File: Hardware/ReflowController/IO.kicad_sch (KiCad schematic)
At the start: 18 parts, among them U5 SZNUD3124DMT1G, U6 VNQ5160K-E

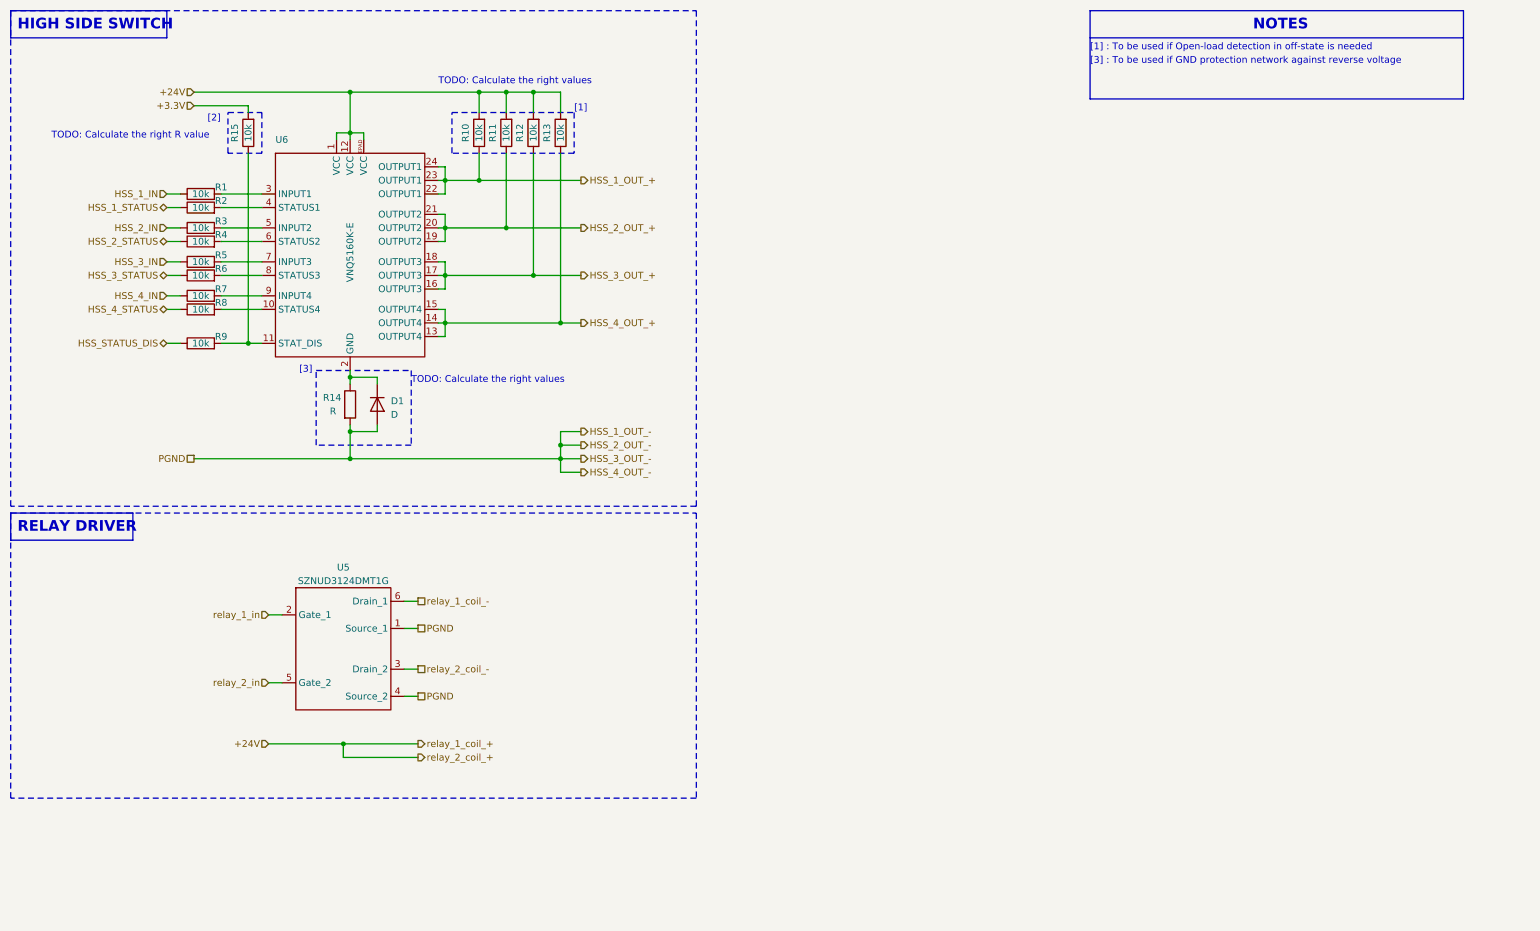
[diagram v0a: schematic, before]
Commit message: added the schematic of the updated pwerAndUi branch(with uC schematic update
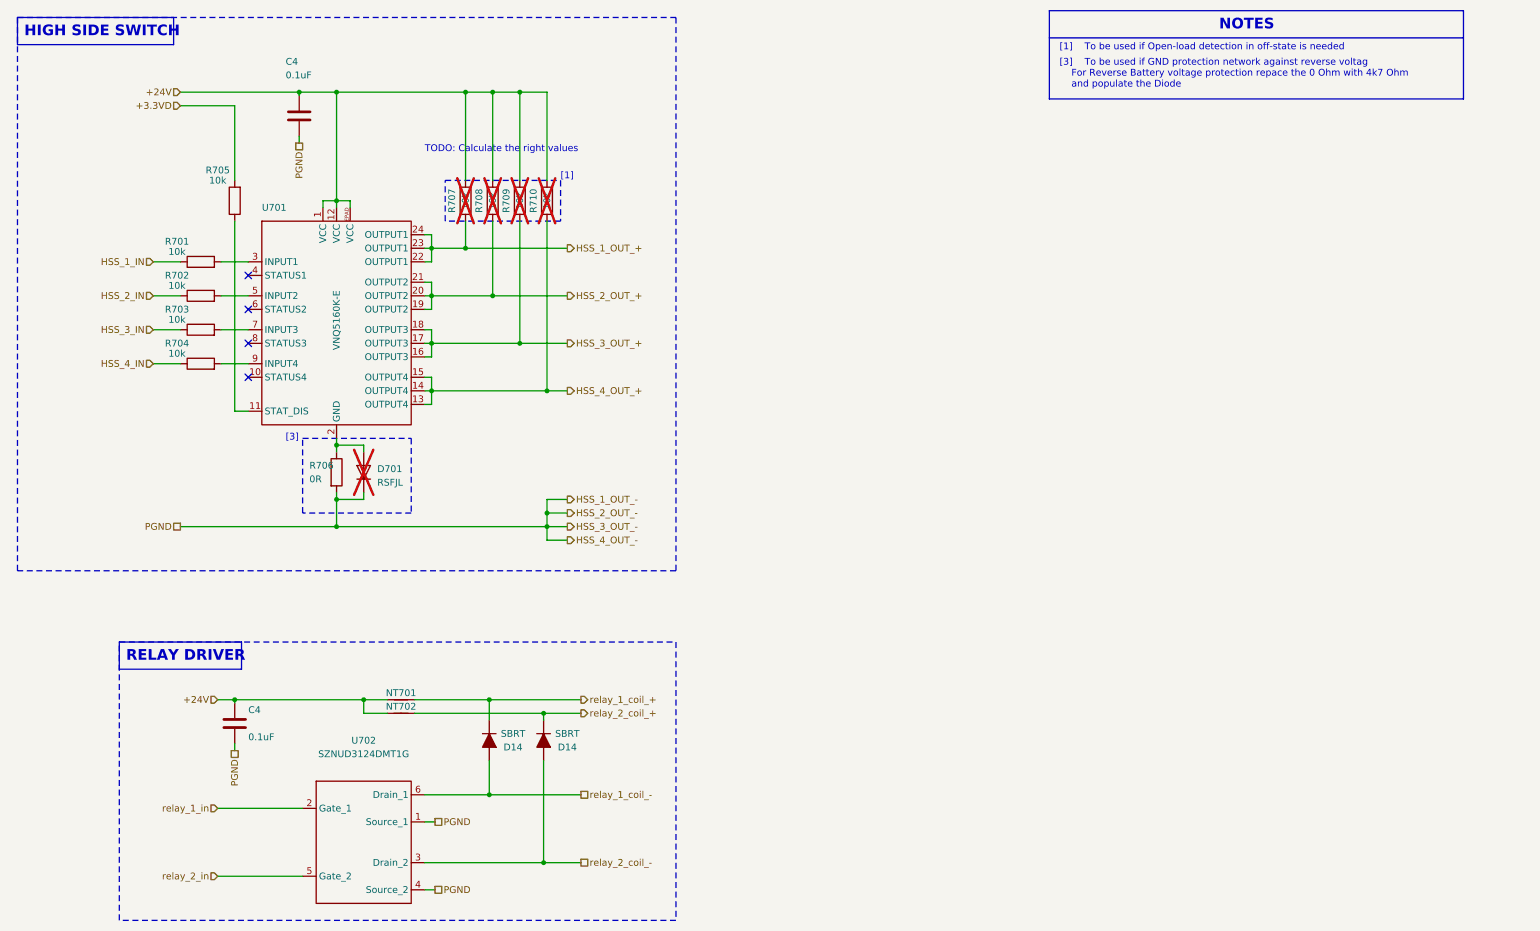
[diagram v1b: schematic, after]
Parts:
- removed R11, R12, R13, R15, R2, R4, R6, R8, R9: 10k, Resistor_SMD:R_0603_1608Metric_Pad0.98x0.95mm_HandSolder, symbol Device:R
- added C4 (x2): 0.1uF, Capacitor_SMD:C_0603_1608Metric_Pad1.08x0.95mm_HandSolder, symbol Device:C
- added D14 (x2): SBRT, Diode_SMD:D_SMA_Handsoldering, symbol Ampli50W-rescue:D_ALT
- added NT701, NT702: NetTie_2, NetTie:NetTie-2_SMD_Pad2.0mm, symbol Device:NetTie_2
- added R705, R708, R709, R710: 10k, Resistor_SMD:R_0603_1608Metric_Pad0.98x0.95mm_HandSolder, symbol Device:R
- D701: renamed from D1; value D -> RSFJL; footprint (none) -> Diode_SMD:D_SMA_Handsoldering; disti (none) -> digikey; disti_no (none) -> 1801-RSFJLTR-ND; man (none) -> taiwan semi; man_no (none) -> RSFJL; now not fitted; now left out of the parts list
- R706: renamed from R14; value R -> 0R; footprint (none) -> Resistor_SMD:R_1206_3216Metric; Field7 (none) -> 13-RC1206FR-134K7LTR-ND; disti (none) -> digikey; man (none) -> yageo; man_no (none) -> RC1206FR-134K7L
- R707: renamed from R10; now not fitted; now left out of the parts list
- renumbered R1 to R701, R3 to R702, R5 to R703, R7 to R704, U6 to U701, U5 to U702
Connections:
- net +24V: now also C4.1, C4.1, NT701.1, NT702.1, R708.2, R709.2, R710.2
- net HSS_1_OUT_-: now also D701.1 (K), C4.2, C4.2; no longer D701.2 (A)
- net HSS_2_OUT_+: now also R708.1
- net HSS_3_OUT_+: now also R709.1
- net HSS_4_OUT_+: now also R710.1
- net relay_1_coil_-: now also D14.2 (A)
- net relay_2_coil_-: now also D14.2 (A)
- net at U701.11 (STAT_DIS): now also R705.1
- net at R706.1, U701.2 (GND): now also D701.2 (A); no longer D701.1 (K)
- new net +3.3VD: R705.2
- new net relay_1_coil_+: D14.1 (K), NT701.2
- new net relay_2_coil_+: D14.1 (K), NT702.2
- no-connect marks 0 -> 4
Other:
- note added: "[1] To be used if Open-load detection in off-state is needed"
- note added: "[3] To be used if GND protection network against reverse voltag For Reverse Battery voltage protection repace the 0 Ohm with 4k7 Ohm and populate the Diode"
- note removed: "TODO: Calculate the right R value"
- note removed: "[1] : To be used if Open-load detection in off-state is needed"
- note removed: "[2]"
- note removed: "[3] : To be used if GND protection network against reverse voltage"
- moved on the sheet: R701, R702, R703, R704, R706, U701, U702
